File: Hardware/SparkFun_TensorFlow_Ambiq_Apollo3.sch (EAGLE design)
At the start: 101 parts, among them J5 CORTEX_DEBUG_PTH, J6 CAMERA-0V7670, M1 MEMS_MIC, M2 MEMS_MIC, U1 AMBIQ-APOLLO3KBR, U2 LIS2DH12, U3 1.8V, U4 LMV358, Y1 32MHz, Y2 32.768kHz

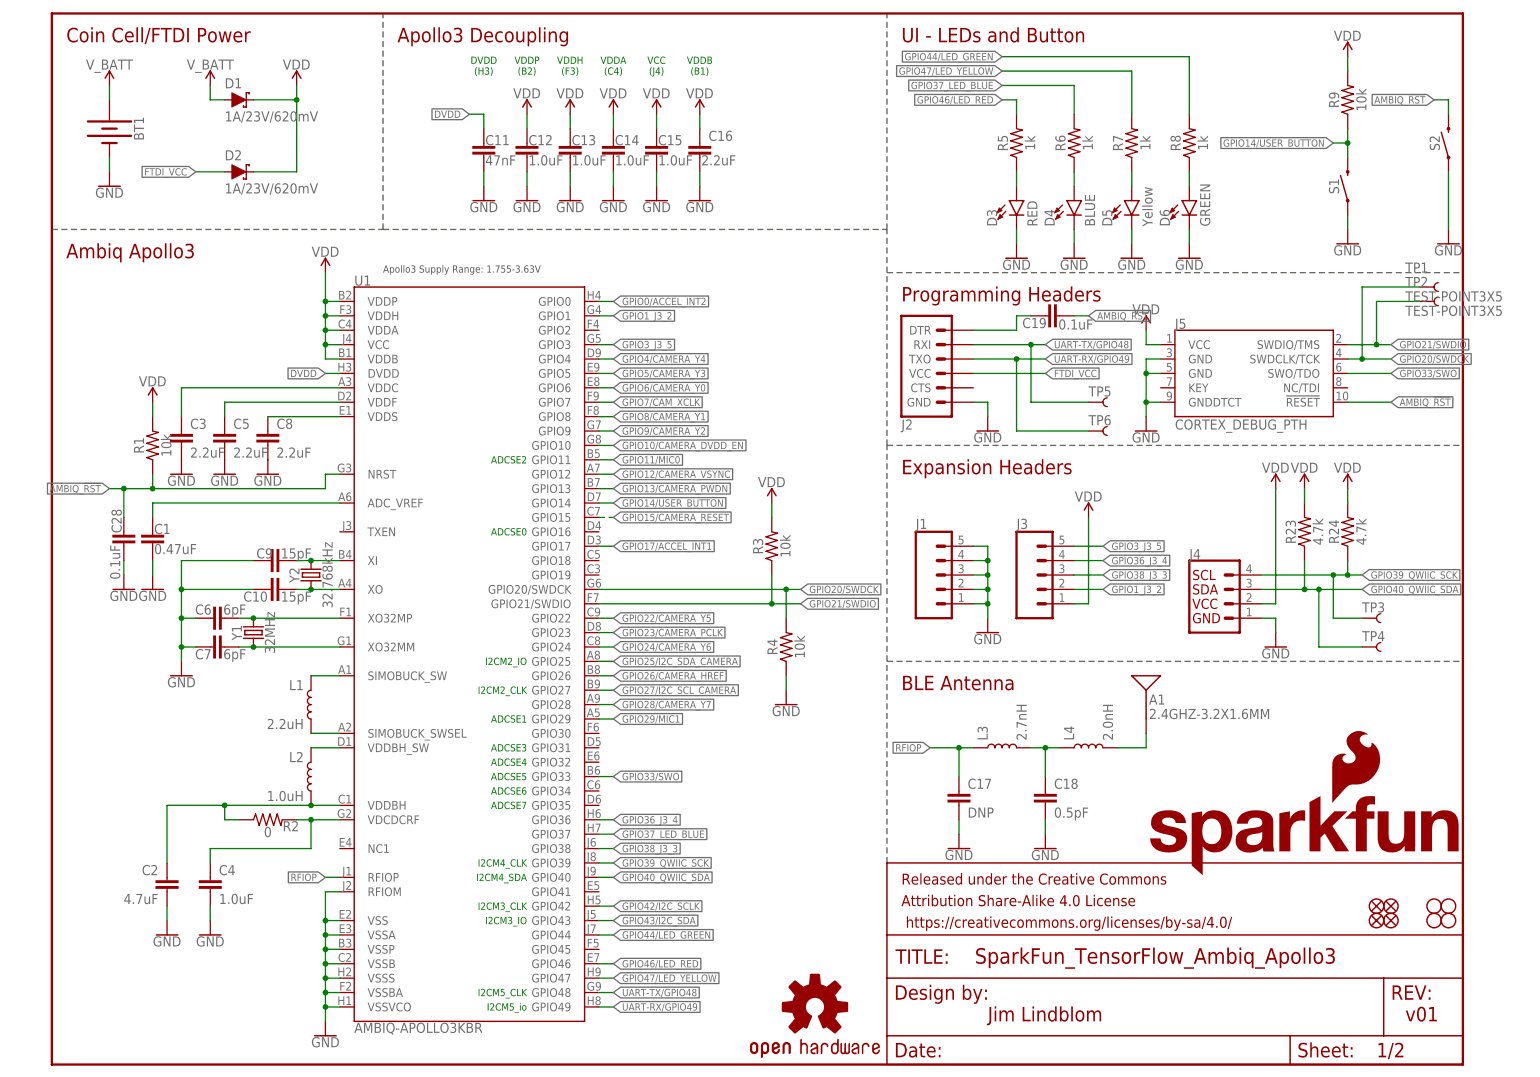
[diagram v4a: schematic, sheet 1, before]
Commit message: Changes post-design review
- Silkscreen on back
- Add auto-reset diode
- Tuck battery overpaste in under connector
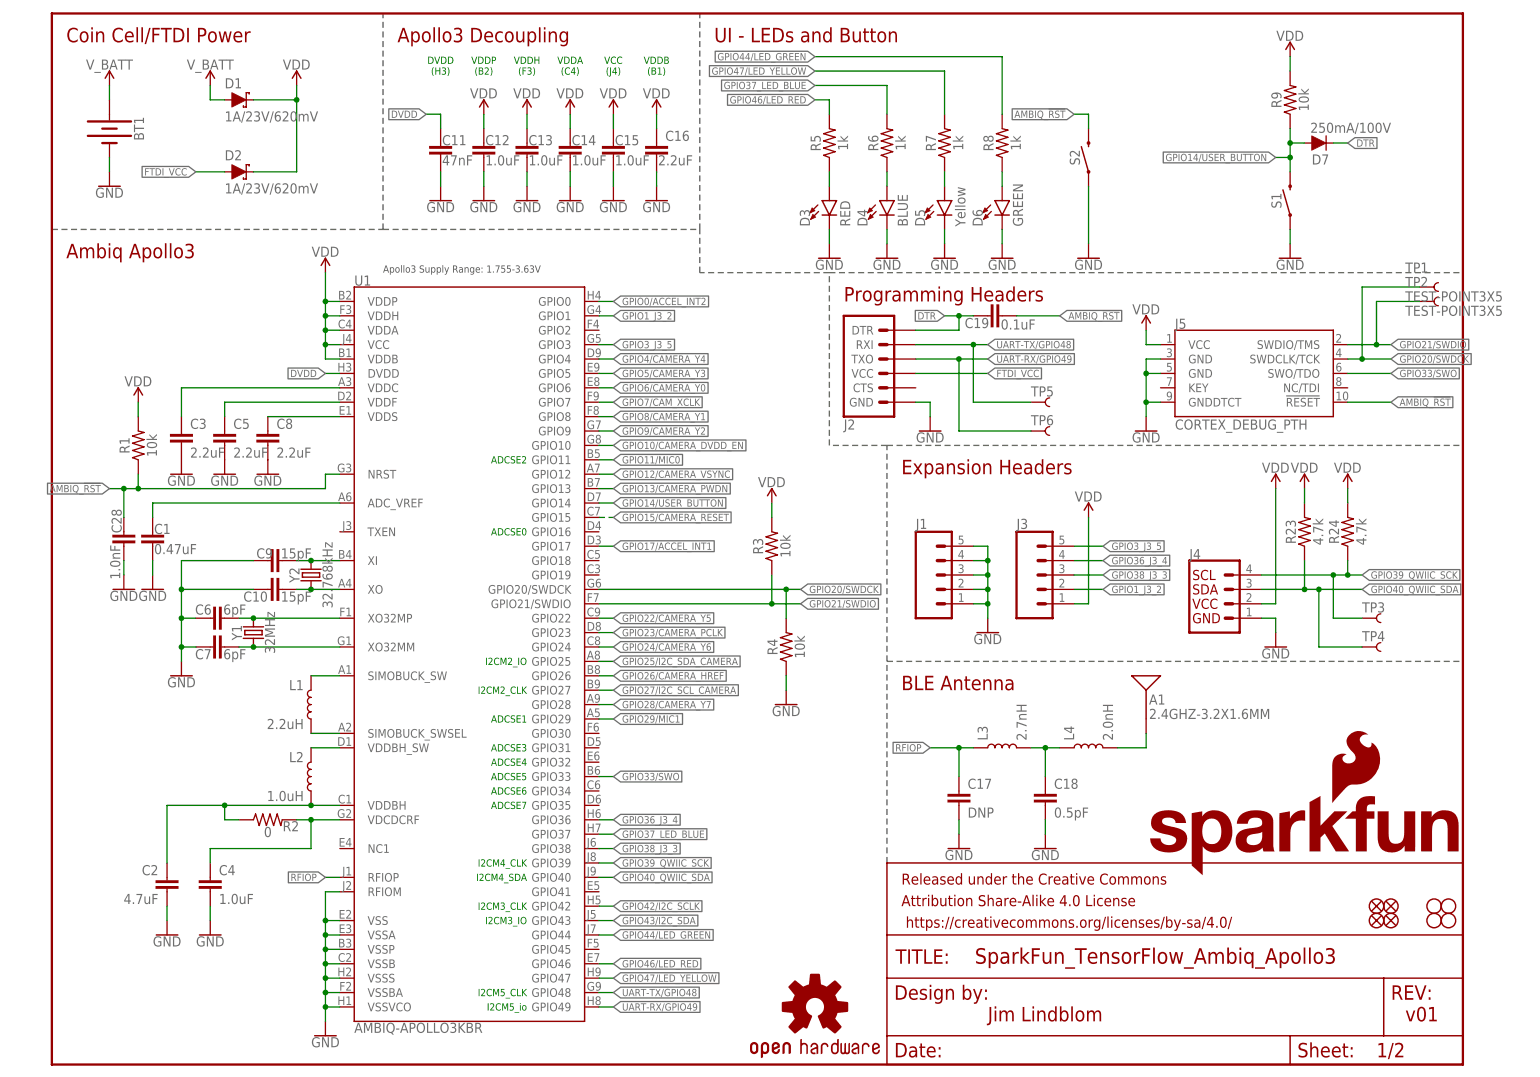
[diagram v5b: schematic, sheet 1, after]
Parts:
- added D7: 250mA/100V, SparkFun-DiscreteSemi:DIODE-BAS16J
- BT1: device SparkFun-Batteries:BATTERY-20MM_SMD_4LEGS_OVERPASTE -> SparkFun-Batteries:BATTERY-20MM_SMD_4LEGS_OVERPASTE_INNER
- C28: value 0.1uF -> 1.0nF; device ambiq:0.1UF-0402-TIGHT-16V-10% -> ambiq:1.0NF/1000PF-0402-50V-10%
- R18: value 10k -> 22k; device ambiq:10KOHM-0402-TIGHT-1/10W-1% -> ambiq:22KOHM-0402-1/16W-1%
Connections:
- removed net N$4: C19.1, J2.DTR
- new net DTR: C19.1, D7.C, J2.DTR
- net GPIO14/USER_BUTTON: now also D7.A
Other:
- moved on the sheet: C11, C12, C13, C14, C15, C16, C19, D3, D4, D5, D6, J2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

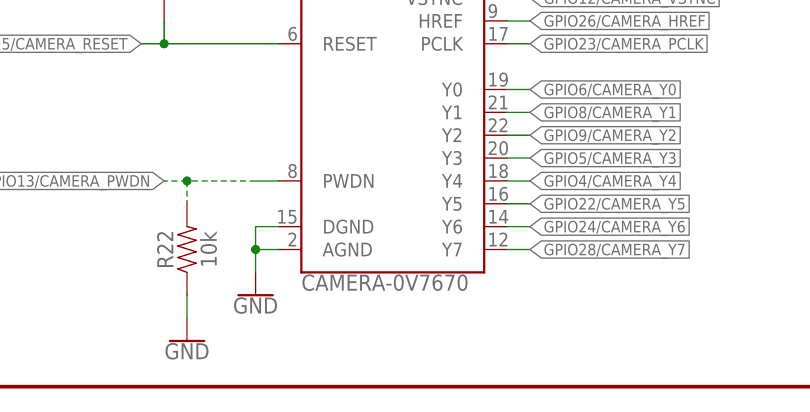
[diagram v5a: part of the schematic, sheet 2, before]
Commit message: Adding production ID's to all part numbers.
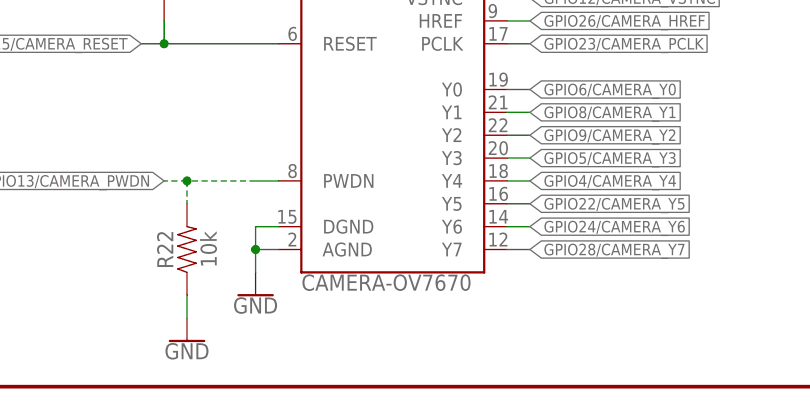
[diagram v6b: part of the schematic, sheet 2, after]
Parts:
- J6: value CAMERA-0V7670 -> CAMERA-OV7670; device ambiq:CAMERA-0V7670 -> ambiq:CAMERA-OV7670
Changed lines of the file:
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@@
 <part name="M1" library="ambiq" deviceset="MEMS_MICROPHONE" device="SPW2430HR5H-B" value="MEMS_MIC"/>
 <part name="M2" library="ambiq" deviceset="MEMS_MICROPHONE" device="SPW2430HR5H-B" value="MEMS_MIC"/>
-<part name="J6" library="ambiq" deviceset="CAMERA-0V7670" device=""/>
+<part name="J6" library="ambiq" deviceset="CAMERA-OV7670" device=""/>
 <part name="BT1" library="SparkFun-Batteries" deviceset="BATTERY" device="-20MM_SMD_4LEGS_OVERPASTE_INNER"/>
 <part name="H4" library="SparkFun-Hardware" deviceset="STAND-OFF" device=""/>

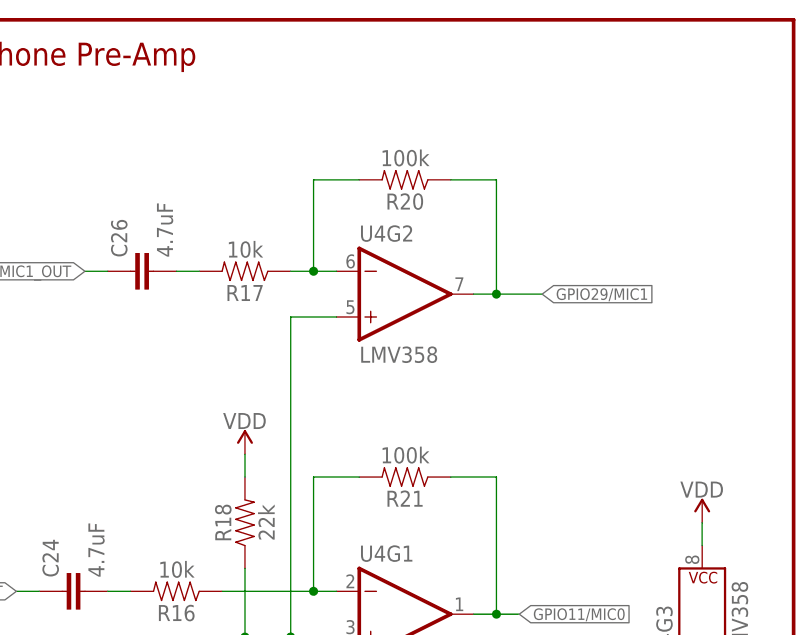
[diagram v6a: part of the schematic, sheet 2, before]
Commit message: Change to 100x gain with 1M ohm resistors for mics
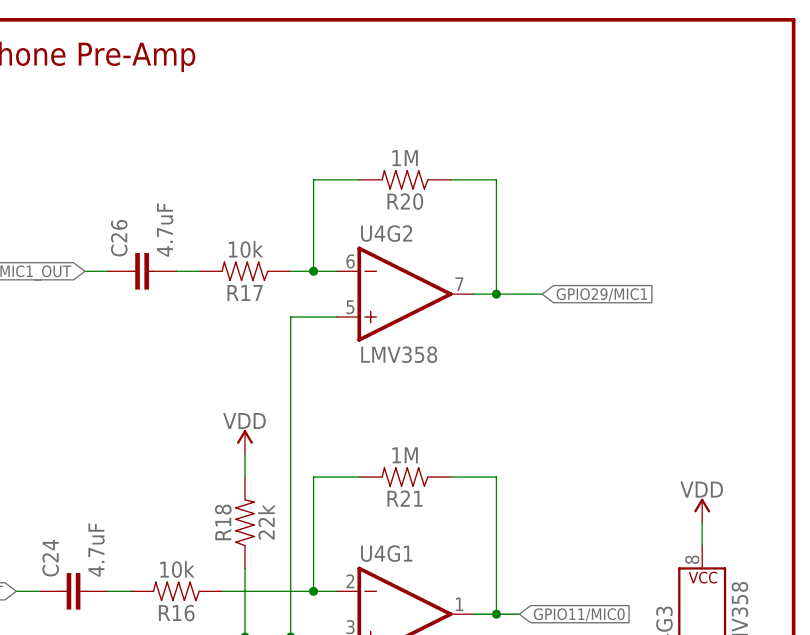
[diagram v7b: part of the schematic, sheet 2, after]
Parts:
- R20, R21: value 100k -> 1M; device SparkFun-Resistors:100KOHM-0603-1/10W-1% -> SparkFun-Resistors:1MOHM-0603-1/4W-5%
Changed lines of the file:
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@@
 <?xml version="1.0" encoding="utf-8"?>
 <!DOCTYPE eagle SYSTEM "eagle.dtd">
-<eagle version="9.2.2">
+<eagle version="9.1.3">
 <drawing>
 <settings>
@@
 <grid distance="0.1" unitdist="inch" unit="inch" style="lines" multiple="1" display="no" altdistance="0.01" altunitdist="inch" altunit="inch"/>
 <layers>
-<layer number="1" name="Top" color="4" fill="1" visible="yes" active="no"/>
-<layer number="2" name="Route2" color="22" fill="3" visible="yes" active="no"/>
-<layer number="15" name="Route15" color="14" fill="6" visible="yes" active="no"/>
-<layer number="16" name="Bottom" color="1" fill="1" visible="yes" active="no"/>
-<layer number="17" name="Pads" color="2" fill="1" visible="yes" active="no"/>
-<layer number="18" name="Vias" color="2" fill="1" visible="yes" active="no"/>
-<layer number="19" name="Unrouted" color="6" fill="1" visible="yes" active="no"/>
-<layer number="20" name="Dimension" color="15" fill="1" visible="yes" active="no"/>
-<layer number="21" name="tPlace" color="16" fill="1" visible="yes" active="no"/>
-<layer number="22" name="bPlace" color="14" fill="1" visible="yes" active="no"/>
-<layer number="23" name="tOrigins" color="15" fill="1" visible="yes" active="no"/>
-<layer number="24" name="bOrigins" color="15" fill="1" visible="yes" active="no"/>
-<layer number="25" name="tNames" color="7" fill="1" visible="yes" active="no"/>
-<layer number="26" name="bNames" color="7" fill="1" visible="yes" active="no"/>
-<layer number="27" name="tValues" color="7" fill="1" visible="yes" active="no"/>
-<layer number="28" name="bValues" color="7" fill="1" visible="yes" active="no"/>
+<layer number="1" name="Top" color="4" fill="1" visible="no" active="no"/>
+<layer number="2" name="Route2" color="22" fill="3" visible="no" active="no"/>
+<layer number="15" name="Route15" color="14" fill="6" visible="no" active="no"/>
+<layer number="16" name="Bottom" color="1" fill="1" visible="no" active="no"/>
+<layer number="17" name="Pads" color="2" fill="1" visible="no" active="no"/>
+<layer number="18" name="Vias" color="2" fill="1" visible="no" active="no"/>
+<layer number="19" name="Unrouted" color="6" fill="1" visible="no" active="no"/>
+<layer number="20" name="Dimension" color="15" fill="1" visible="no" active="no"/>
+<layer number="21" name="tPlace" color="16" fill="1" visible="no" active="no"/>
+<layer number="22" name="bPlace" color="14" fill="1" visible="no" active="no"/>
+<layer number="23" name="tOrigins" color="15" fill="1" visible="no" active="no"/>
+<layer number="24" name="bOrigins" color="15" fill="1" visible="no" active="no"/>
+<layer number="25" name="tNames" color="7" fill="1" visible="no" active="no"/>
+<layer number="26" name="bNames" color="7" fill="1" visible="no" active="no"/>
+<layer number="27" name="tValues" color="7" fill="1" visible="no" active="no"/>
+<layer number="28" name="bValues" color="7" fill="1" visible="no" active="no"/>
 <layer number="29" name="tStop" color="7" fill="3" visible="no" active="no"/>
 <layer number="30" name="bStop" color="7" fill="6" visible="no" active="no"/>
@@
 <layer number="35" name="tGlue" color="7" fill="4" visible="no" active="no"/>
 <layer number="36" name="bGlue" color="7" fill="5" visible="no" active="no"/>
-<layer number="37" name="tTest" color="7" fill="1" visible="yes" active="no"/>
-<layer number="38" name="bTest" color="7" fill="1" visible="yes" active="no"/>
+<layer number="37" name="tTest" color="7" fill="1" visible="no" active="no"/>
+<layer number="38" name="bTest" color="7" fill="1" visible="no" active="no"/>
 <layer number="39" name="tKeepout" color="4" fill="11" visible="no" active="no"/>
 <layer number="40" name="bKeepout" color="1" fill="11" visible="no" active="no"/>
@@
 <layer number="44" name="Drills" color="7" fill="1" visible="no" active="no"/>
 <layer number="45" name="Holes" color="7" fill="1" visible="no" active="no"/>
-<layer number="46" name="Milling" color="3" fill="1" visible="yes" active="no"/>
-<layer number="47" name="Measures" color="7" fill="1" visible="yes" active="no"/>
-<layer number="48" name="Document" color="7" fill="1" visible="yes" active="no"/>
-<layer number="49" name="Reference" color="7" fill="1" visible="yes" active="no"/>
-<layer number="50" name="dxf" color="7" fill="1" visible="yes" active="no"/>
-<layer number="51" name="tDocu" color="6" fill="1" visible="yes" active="no"/>
-<layer number="52" name="bDocu" color="7" fill="1" visible="yes" active="no"/>
-<layer number="53" name="tGND_GNDA" color="7" fill="9" visible="yes" active="no"/>
-<layer number="54" name="bGND_GNDA" color="1" fill="9" visible="yes" active="no"/>
-<layer number="56" name="wert" color="7" fill="1" visible="yes" active="no"/>
-<layer number="57" name="tCAD" color="7" fill="1" visible="yes" active="no"/>
-<layer number="59" name="tCarbon" color="7" fill="1" visible="yes" active="no"/>
-<layer number="60" name="bCarbon" color="7" fill="1" visible="yes" active="no"/>
+<layer number="46" name="Milling" color="3" fill="1" visible="no" active="no"/>
+<layer number="47" name="Measures" color="7" fill="1" visible="no" active="no"/>
+<layer number="48" name="Document" color="7" fill="1" visible="no" active="no"/>
+<layer number="49" name="Reference" color="7" fill="1" visible="no" active="no"/>
+<layer number="50" name="dxf" color="7" fill="1" visible="no" active="no"/>
+<layer number="51" name="tDocu" color="6" fill="1" visible="no" active="no"/>
+<layer number="52" name="bDocu" color="7" fill="1" visible="no" active="no"/>
+<layer number="53" name="tGND_GNDA" color="7" fill="9" visible="no" active="no"/>
+<layer number="54" name="bGND_GNDA" color="1" fill="9" visible="no" active="no"/>
+<layer number="56" name="wert" color="7" fill="1" visible="no" active="no"/>
+<layer number="57" name="tCAD" color="7" fill="1" visible="no" active="no"/>
+<layer number="59" name="tCarbon" color="7" fill="1" visible="no" active="no"/>
+<layer number="60" name="bCarbon" color="7" fill="1" visible="no" active="no"/>
 <layer number="88" name="SimResults" color="9" fill="1" visible="yes" active="yes"/>
 <layer number="89" name="SimProbes" color="9" fill="1" visible="yes" active="yes"/>
@@
 <part name="GND37" library="SparkFun-PowerSymbols" deviceset="GND" device=""/>
 <part name="R16" library="SparkFun-Resistors" deviceset="10KOHM" device="-0603-1/10W-1%" value="10k"/>
-<part name="R21" library="SparkFun-Resistors" deviceset="100KOHM" device="-0603-1/10W-1%" value="100k"/>
+<part name="R21" library="SparkFun-Resistors" deviceset="1MOHM" device="-0603-1/4W-5%" value="1M"/>
 <part name="SUPPLY34" library="SparkFun-PowerSymbols" deviceset="VDD" device=""/>
 <part name="GND39" library="SparkFun-PowerSymbols" deviceset="GND" device=""/>
@@
 <part name="U4" library="SparkFun-IC-Amplifiers" deviceset="LMV358" device="SOIC" value="LMV358"/>
 <part name="R17" library="SparkFun-Resistors" deviceset="10KOHM" device="-0603-1/10W-1%" value="10k"/>
-<part name="R20" library="SparkFun-Resistors" deviceset="100KOHM" device="-0603-1/10W-1%" value="100k"/>
+<part name="R20" library="SparkFun-Resistors" deviceset="1MOHM" device="-0603-1/4W-5%" value="1M"/>
 <part name="C26" library="SparkFun-Capacitors" deviceset="4.7UF" device="-0603-6.3V-(10%)" value="4.7uF"/>
 <part name="J3" library="SparkFun-Connectors" deviceset="CONN_05" device="NO_SILK"/>

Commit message: Change Mic gain to 75x
This is Pete's requested final gain value
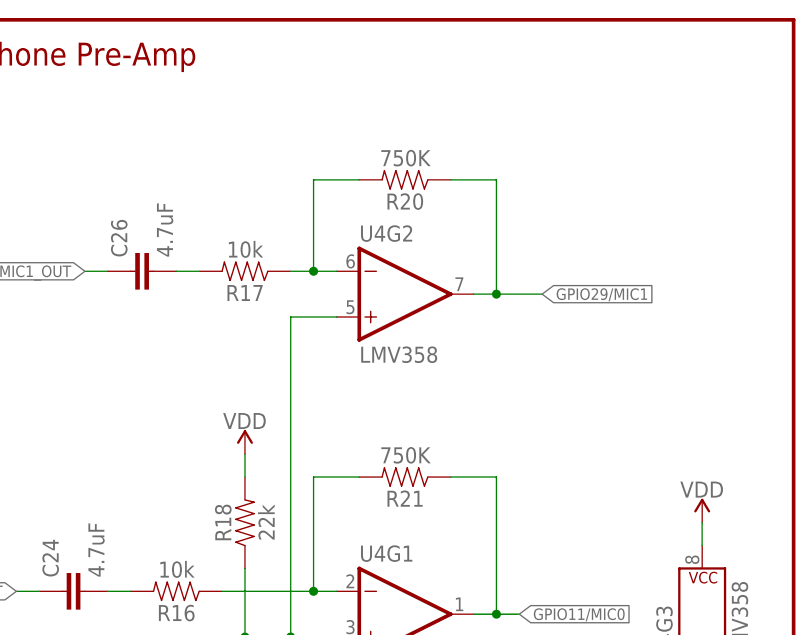
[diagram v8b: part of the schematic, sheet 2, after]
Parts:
- R20, R21: value 1M -> 750K; device SparkFun-Resistors:1MOHM-0603-1/4W-5% -> SparkFun-Resistors:750KOHM-0603-1/10W-1%
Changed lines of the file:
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@@
 <part name="GND37" library="SparkFun-PowerSymbols" deviceset="GND" device=""/>
 <part name="R16" library="SparkFun-Resistors" deviceset="10KOHM" device="-0603-1/10W-1%" value="10k"/>
-<part name="R21" library="SparkFun-Resistors" deviceset="1MOHM" device="-0603-1/4W-5%" value="1M"/>
+<part name="R21" library="SparkFun-Resistors" deviceset="750KOHM" device="-0603-1/10W-1%" value="750K"/>
 <part name="SUPPLY34" library="SparkFun-PowerSymbols" deviceset="VDD" device=""/>
 <part name="GND39" library="SparkFun-PowerSymbols" deviceset="GND" device=""/>
@@
 <part name="U4" library="SparkFun-IC-Amplifiers" deviceset="LMV358" device="SOIC" value="LMV358"/>
 <part name="R17" library="SparkFun-Resistors" deviceset="10KOHM" device="-0603-1/10W-1%" value="10k"/>
-<part name="R20" library="SparkFun-Resistors" deviceset="1MOHM" device="-0603-1/4W-5%" value="1M"/>
+<part name="R20" library="SparkFun-Resistors" deviceset="750KOHM" device="-0603-1/10W-1%" value="750K"/>
 <part name="C26" library="SparkFun-Capacitors" deviceset="4.7UF" device="-0603-6.3V-(10%)" value="4.7uF"/>
 <part name="J3" library="SparkFun-Connectors" deviceset="CONN_05" device="NO_SILK"/>
